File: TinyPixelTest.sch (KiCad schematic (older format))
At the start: 40 parts, among them IC1 ATTINY2313-S

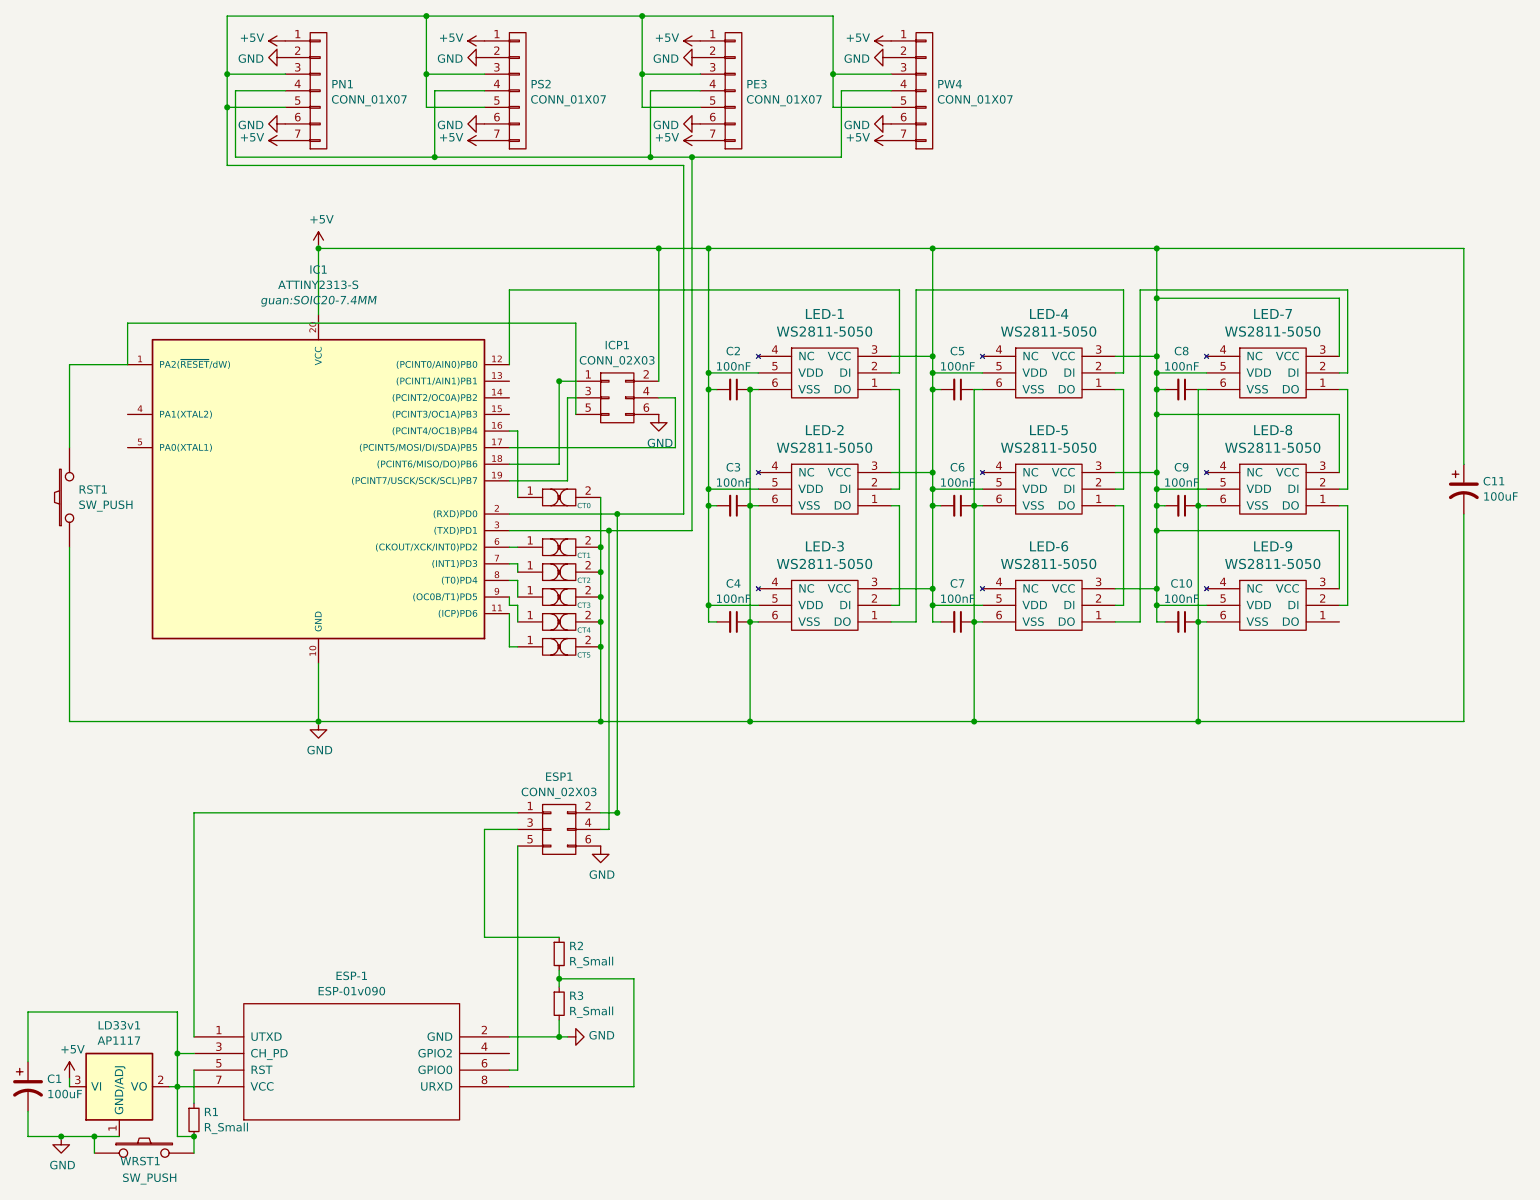
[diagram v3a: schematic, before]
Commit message: Fixed reset switch
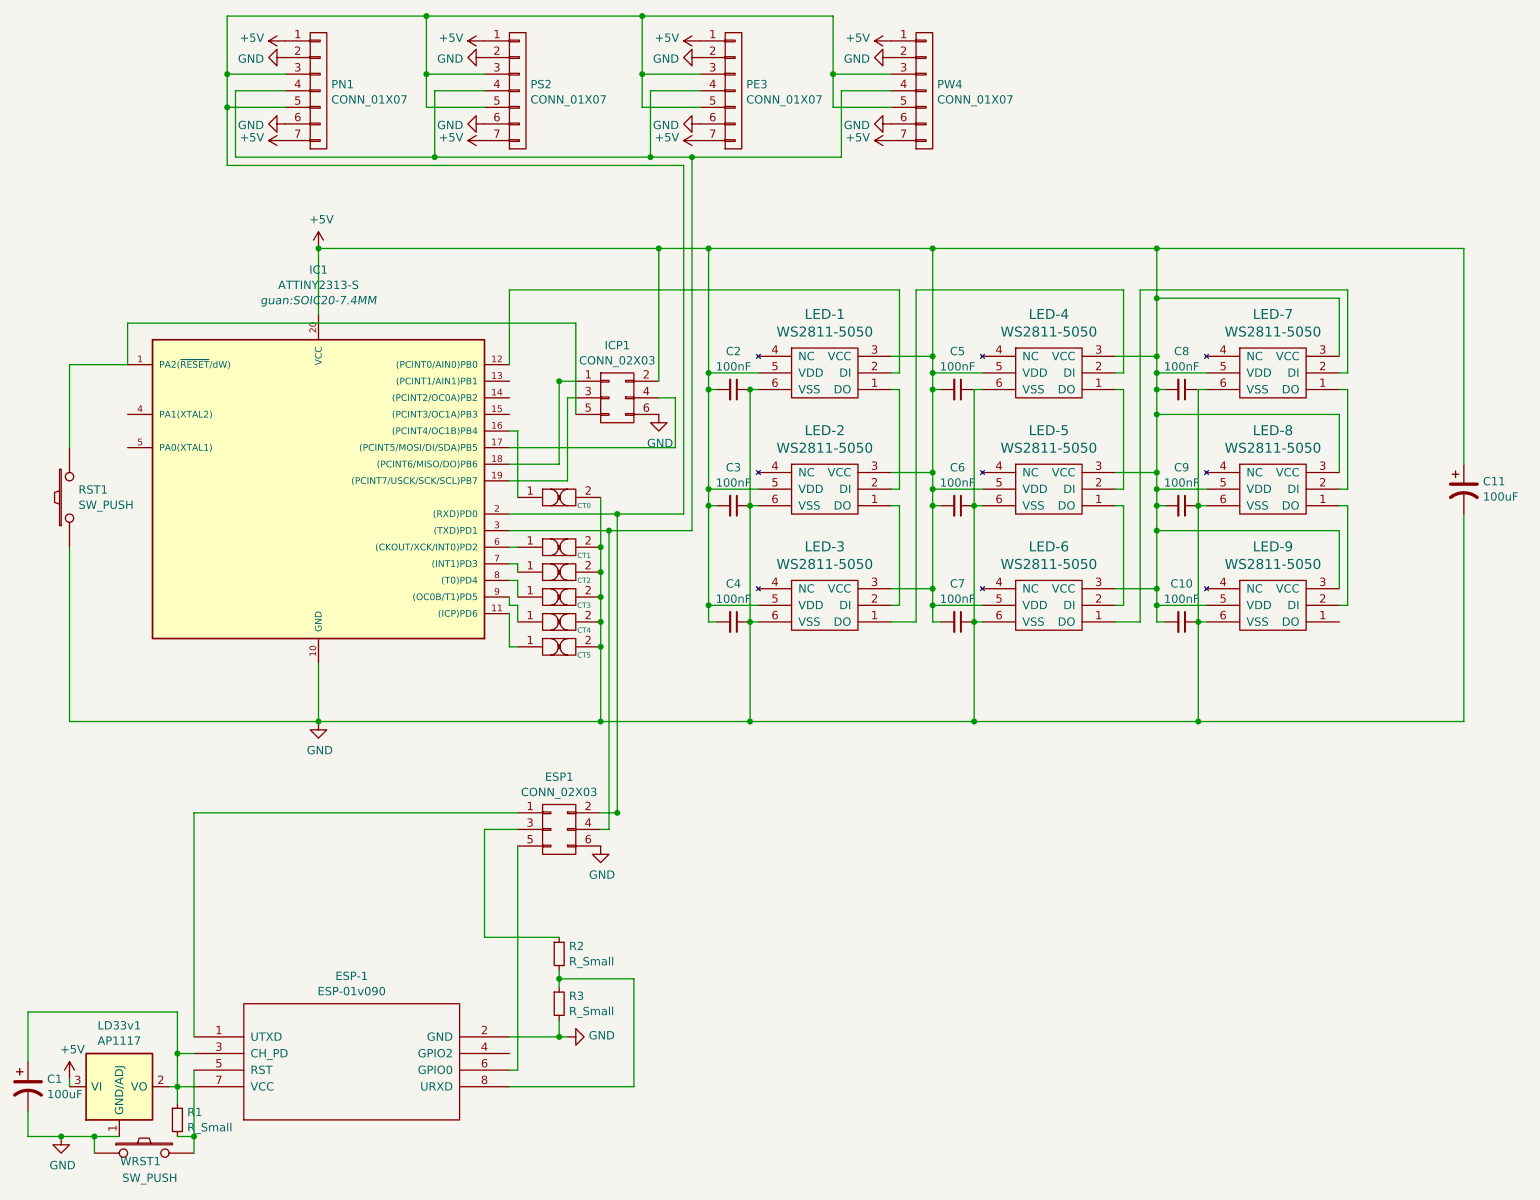
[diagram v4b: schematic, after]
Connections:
- net at C1.1, ESP-1.3 (CH_PD), ESP-1.7 (VCC)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: now also R1.1; no longer R1.2, WRST1.2
- net at ESP-1.5 (RST): now also R1.2, WRST1.2; no longer R1.1
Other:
- moved on the sheet: R1
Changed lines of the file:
@@
 L R_Small R1
 U 1 1 56A54D88
-P 1650 7200
-F 0 "R1" H 1709 7246 50  0000 L CNN
-F 1 "R_Small" H 1709 7154 50  0000 L CNN
-F 2 "Resistors_SMD:R_0603_HandSoldering" H 1650 7200 50  0001 C CNN
-F 3 "" H 1650 7200 50  0000 C CNN
-	1    1650 7200
+P 1550 7200
+F 0 "R1" H 1609 7246 50  0000 L CNN
+F 1 "R_Small" H 1609 7154 50  0000 L CNN
+F 2 "Resistors_SMD:R_0603_HandSoldering" H 1550 7200 50  0001 C CNN
+F 3 "" H 1550 7200 50  0000 C CNN
+	1    1550 7200
 	1    0    0    -1
 $EndComp
@@
 $EndComp
 Wire Wire Line
-	4750 1950 4750 2700
-Wire Wire Line
-	4750 2700 4750 2800
-Wire Wire Line
-	4750 2800 4750 3400
-Wire Wire Line
-	4750 3400 4750 3500
-Wire Wire Line
-	4750 3500 4750 4100
-Wire Wire Line
-	4750 4100 4750 4200
+	4750 1950 4750 4200
 Wire Wire Line
 	4750 4100 5050 4100
@@
 Connection ~ 4750 2700
 Wire Wire Line
-	6100 1950 6100 2600
-Wire Wire Line
-	6100 2600 6100 2700
-Wire Wire Line
-	6100 2700 6100 2800
-Wire Wire Line
-	6100 2800 6100 3300
-Wire Wire Line
-	6100 3300 6100 3400
-Wire Wire Line
-	6100 3400 6100 3500
-Wire Wire Line
-	6100 3500 6100 4000
-Wire Wire Line
-	6100 4000 6100 4100
-Wire Wire Line
-	6100 4100 6100 4200
+	6100 1950 6100 4200
 Wire Wire Line
 	6100 4100 6400 4100
@@
 Connection ~ 6100 3400
 Wire Wire Line
-	7450 1950 7450 2250
-Wire Wire Line
-	7450 2250 7450 2600
-Wire Wire Line
-	7450 2600 7450 2700
-Wire Wire Line
-	7450 2700 7450 2800
-Wire Wire Line
-	7450 2800 7450 2950
-Wire Wire Line
-	7450 2950 7450 3300
-Wire Wire Line
-	7450 3300 7450 3400
-Wire Wire Line
-	7450 3400 7450 3500
-Wire Wire Line
-	7450 3500 7450 3650
-Wire Wire Line
-	7450 3650 7450 4000
-Wire Wire Line
-	7450 4000 7450 4100
-Wire Wire Line
-	7450 4100 7450 4200
+	7450 1950 7450 4200
 Wire Wire Line
 	7450 4100 7750 4100
@@
 Connection ~ 7450 2700
 Wire Wire Line
-	2400 1950 4450 1950
-Wire Wire Line
-	4450 1950 4750 1950
-Wire Wire Line
-	4750 1950 6100 1950
-Wire Wire Line
-	6100 1950 7450 1950
-Wire Wire Line
-	7450 1950 9300 1950
+	2400 1950 9300 1950
 Connection ~ 6100 1950
 Wire Wire Line
 	5000 2800 5050 2800
 Wire Wire Line
-	5000 4800 5000 4200
-Wire Wire Line
-	5000 4200 5000 3500
-Wire Wire Line
-	5000 3500 5000 2800
+	5000 4800 5000 2800
 Wire Wire Line
 	5050 3500 5000 3500
@@
 Connection ~ 5000 4200
 Wire Wire Line
-	6350 4800 6350 4200
-Wire Wire Line
-	6350 4200 6350 3500
-Wire Wire Line
-	6350 3500 6350 2800
+	6350 4800 6350 2800
 Wire Wire Line
 	6350 2800 6400 2800
@@
 Connection ~ 6350 4200
 Wire Wire Line
-	7700 4800 7700 4200
-Wire Wire Line
-	7700 4200 7700 3500
-Wire Wire Line
-	7700 3500 7700 2800
+	7700 4800 7700 2800
 Wire Wire Line
 	7700 2800 7750 2800
@@
 Connection ~ 7700 4200
 Wire Wire Line
-	900  4800 2400 4800
-Wire Wire Line
-	2400 4800 4100 4800
-Wire Wire Line
-	4100 4800 5000 4800
-Wire Wire Line
-	5000 4800 6350 4800
-Wire Wire Line
-	6350 4800 7700 4800
-Wire Wire Line
-	7700 4800 9300 4800
+	900  4800 9300 4800
 Connection ~ 6350 4800
 Wire Wire Line
@@
 	900  7000 900  6950
 Wire Wire Line
-	3550 6700 3850 6700
-Wire Wire Line
-	3850 6700 3900 6700
+	3550 6700 3900 6700
 Wire Wire Line
 	1650 5350 1650 6700
 Wire Wire Line
-	3550 3550 4200 3550
-Wire Wire Line
-	4200 3550 4600 3550
-Wire Wire Line
-	650  7300 850  7300
-Wire Wire Line
-	850  7300 1050 7300
-Wire Wire Line
-	1050 7300 1200 7300
+	3550 3550 4600 3550
+Wire Wire Line
+	650  7300 1200 7300
 Wire Wire Line
 	1650 5350 3600 5350
@@
 Connection ~ 3850 6700
 Wire Wire Line
-	3850 6300 3850 6350
-Wire Wire Line
-	3850 6350 3850 6400
+	3850 6300 3850 6400
 Wire Wire Line
 	3850 6350 4300 6350
@@
 Connection ~ 850  7300
 Wire Wire Line
-	1500 7000 1550 7000
-Wire Wire Line
-	1550 7000 1650 7000
+	1500 7000 1650 7000
 Connection ~ 1650 7300
 Wire Wire Line
 	650  7300 650  7150
 Wire Wire Line
-	1650 6900 1650 7100
-Wire Wire Line
-	1550 7300 1650 7300
-Wire Wire Line
-	1550 6550 1550 6800
-Wire Wire Line
-	1550 6800 1550 7000
-Wire Wire Line
-	1550 7000 1550 7300
+	1650 6900 1650 7400
+Wire Wire Line
+	1550 6550 1550 7100
 Connection ~ 1550 7000
 Wire Wire Line
@@
 	1050 7400 1050 7300
 Connection ~ 1050 7300
-Wire Wire Line
-	1650 7300 1650 7400
 $Comp
 L CUT-1 CT1
@@
 $EndComp
 Wire Wire Line
-	3550 3650 4150 3650
-Wire Wire Line
-	4150 3650 4650 3650
+	3550 3650 4650 3650
 $Comp
 L CUT-1 CT2
@@
 	3550 4350 3600 4350
 Wire Wire Line
-	4100 3450 4100 3750
-Wire Wire Line
-	4100 3750 4100 3900
-Wire Wire Line
-	4100 3900 4100 4050
-Wire Wire Line
-	4100 4050 4100 4200
-Wire Wire Line
-	4100 4200 4100 4350
-Wire Wire Line
-	4100 4350 4100 4800
+	4100 3450 4100 4800
 Connection ~ 4100 4800
 Connection ~ 4100 4350
@@
 Connection ~ 4150 3650
 Wire Wire Line
-	4600 1450 4600 3550
-Wire Wire Line
-	1850 1450 4600 1450
+	4600 3550 4600 1450
+Wire Wire Line
+	4600 1450 1850 1450
 Connection ~ 4200 3550
 $Comp
@@
 	4700 900  4350 900
 Wire Wire Line
-	4350 550  4350 900
-Wire Wire Line
-	4350 900  4350 1100
-Wire Wire Line
-	1850 550  3050 550
-Wire Wire Line
-	3050 550  4350 550
-Wire Wire Line
-	4350 550  5500 550
-Wire Wire Line
-	1850 550  1850 900
-Wire Wire Line
-	1850 900  1850 1100
-Wire Wire Line
-	1850 1100 1850 1450
+	4350 550  4350 1100
+Wire Wire Line
+	1850 550  5500 550
+Wire Wire Line
+	1850 1450 1850 550
 Wire Wire Line
 	1850 900  2200 900
 Wire Wire Line
-	3050 550  3050 900
-Wire Wire Line
-	3050 900  3050 1100
+	3050 550  3050 1100
 Wire Wire Line
 	3050 900  3400 900
 Connection ~ 3050 550
 Wire Wire Line
-	5500 550  5500 900
-Wire Wire Line
-	5500 900  5500 1100
+	5500 550  5500 1100
 Wire Wire Line
 	5500 900  5850 900
@@
 	5850 1000 5550 1000
 Wire Wire Line
-	5550 1400 5550 1000
-Wire Wire Line
-	1900 1400 3100 1400
-Wire Wire Line
-	3100 1400 4400 1400
-Wire Wire Line
-	4400 1400 4650 1400
-Wire Wire Line
-	4650 1400 5550 1400
+	5550 1000 5550 1400
+Wire Wire Line
+	5550 1400 1900 1400
 Wire Wire Line
 	1900 1400 1900 1000
@@
 $EndComp
 Connection ~ 1850 1100
+Wire Wire Line
+	1650 7300 1550 7300
 $EndSCHEMATC
